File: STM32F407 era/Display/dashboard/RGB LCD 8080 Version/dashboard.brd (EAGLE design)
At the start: 200 x 75.1 mm, 89 parts, among them IC2 74HC14D, IC3 74HC14D, U1 CAT4238TD-GT3

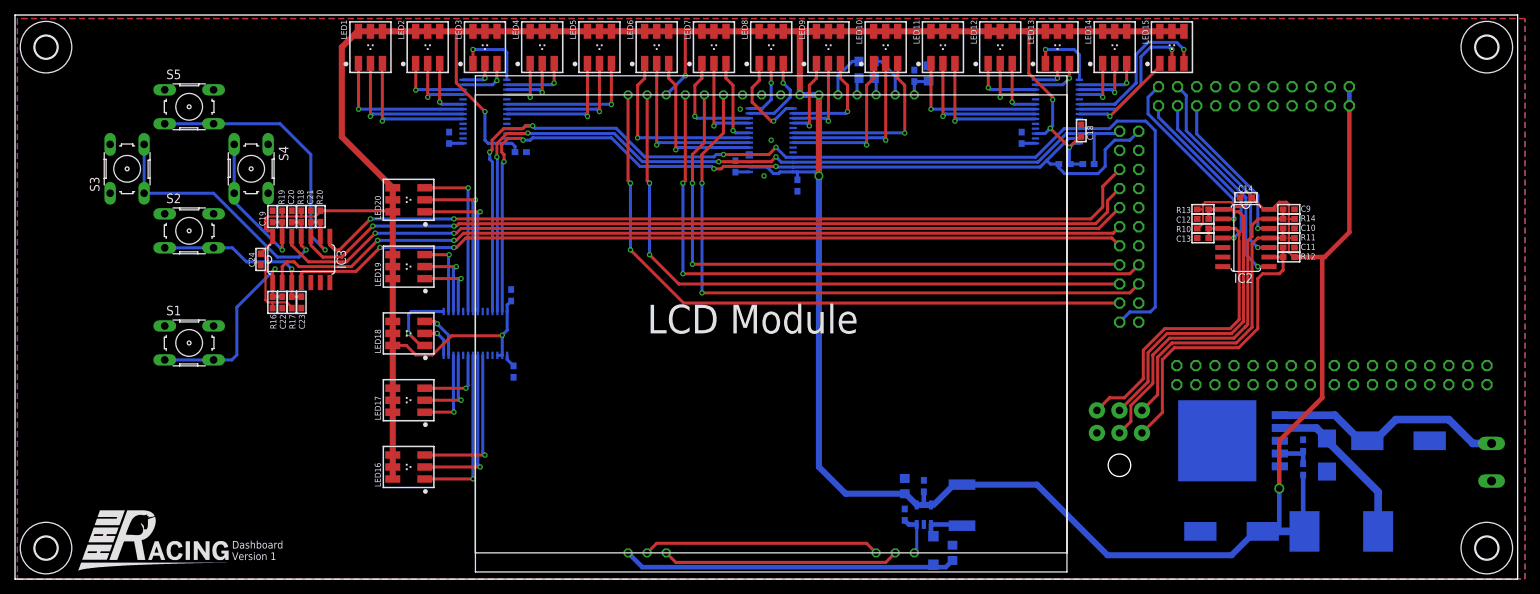
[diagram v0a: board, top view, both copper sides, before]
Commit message: started work on alternativ LCD solution
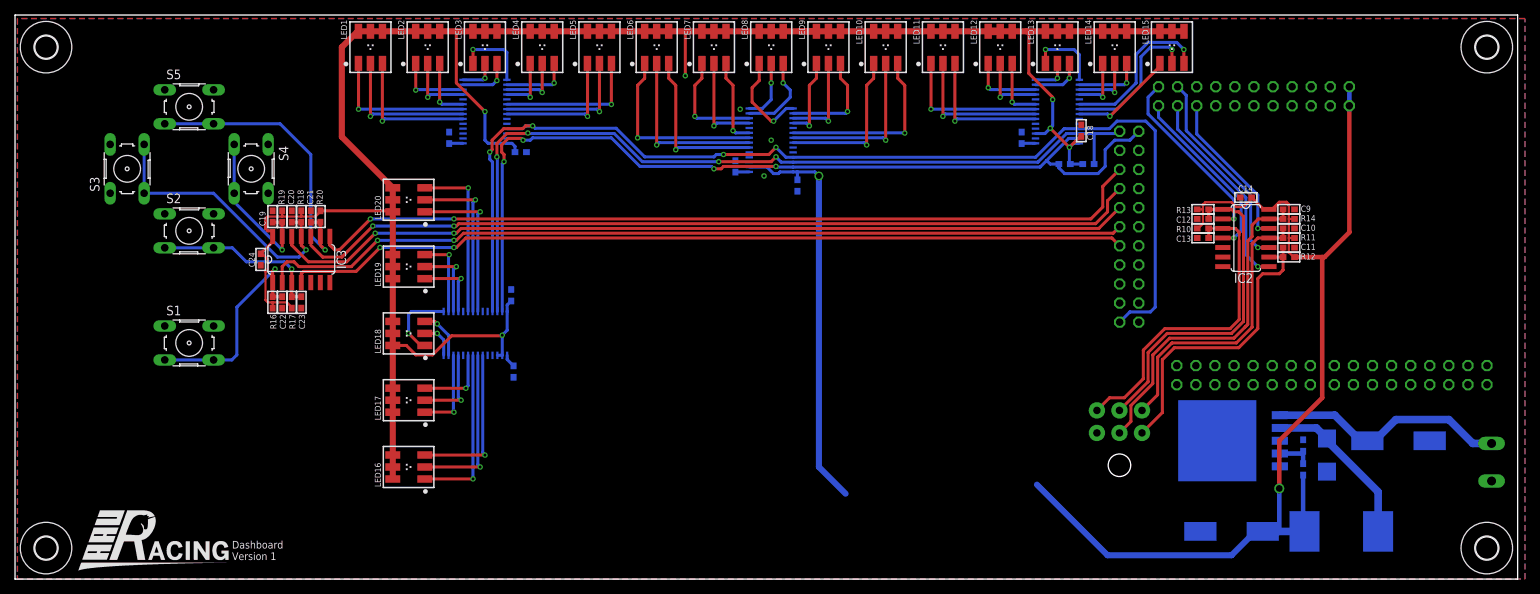
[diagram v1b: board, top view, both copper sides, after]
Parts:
- removed C1: 220n, microbuilder:_0805
- removed C2: 1u, microbuilder:_0805
- removed C3, C8: 100n, microbuilder:_0603
- removed C6, C7: 2u, microbuilder:_0805
- removed D1: MBR0520LT, diode:SOD123
- removed L1: WE-PD4S, WE-PD4:S
- removed R1: 15, microbuilder:_0603
- removed R9: 10m, microbuilder:_0805
- removed U$10: EA-DOGXL160W-7, unicorn_v2:EA-DOGXL160W-7
- removed U1: CAT4238TD-GT3, microbuilder:SOT23-5
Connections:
- removed net N$1: U$10.P$14, U$10.P$2
- removed net N$2: U$10.P$15, U$10.P$3
- removed net N$3: R1.1, U$10.P$16, U1.3
- removed net N$4: C1.1, D1.C, U$10.P$1
- removed net N$5: D1.A, L1.1, U1.1
- removed net N$57: C6.1, U$10.P$20
- removed net N$58: C7.1, U$10.P$21
- removed net N$59: C6.2, U$10.P$19
- removed net N$60: C7.2, U$10.P$18
- removed net N$61: C8.2, R9.2, U$10.P$17
- net 3.3V: no longer C2.1, C3.1, L1.2, U$10.P$22, U$10.P$23, U$10.P$30, U1.4, U1.5
- net CD: no longer U$10.P$27
- net GND: no longer C1.2, C2.2, C3.2, C8.1, R1.2, R9.1, U$10.P$24, U$10.P$25, U$10.P$26, U1.2
- net LCD_CLOCK: no longer U$10.P$32
- net LCD_CS: no longer U$10.P$28
- net LCD_DATA: no longer U$10.P$31
- net LCD_RESET: no longer U$10.P$29
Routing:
- net LCD_CLOCK: track 88.8 -> 0.00 mm, vias 2 -> 0
- net CD: track 86.2 -> 0.00 mm, vias 2 -> 0
- net LCD_DATA: track 85.6 -> 0.00 mm, vias 2 -> 0
- net LCD_RESET: track 85.1 -> 0.00 mm, vias 2 -> 0
- net LCD_CS: track 80.1 -> 0.00 mm, vias 2 -> 0
- net 3.3V: track 543.4 -> 489.1 mm
- net N$4: track 44.6 -> 0.00 mm
- net N$2: track 31.5 -> 0.00 mm
- net N$1: track 31.5 -> 0.00 mm
- net N$60: track 6.12 -> 0.00 mm
- net N$58: track 6.12 -> 0.00 mm
- net N$5: track 6.08 -> 0.00 mm
- net N$3: track 5.73 -> 0.00 mm
- net N$61: track 3.71 -> 0.00 mm
- net N$59: track 2.48 -> 0.00 mm
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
